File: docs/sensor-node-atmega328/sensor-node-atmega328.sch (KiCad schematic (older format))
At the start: 11 parts, among them IC1 ATMEGA328-P, P1 CONN_01X06, SW1 SPST, U1 HTU21D, U2 nRF24L01+

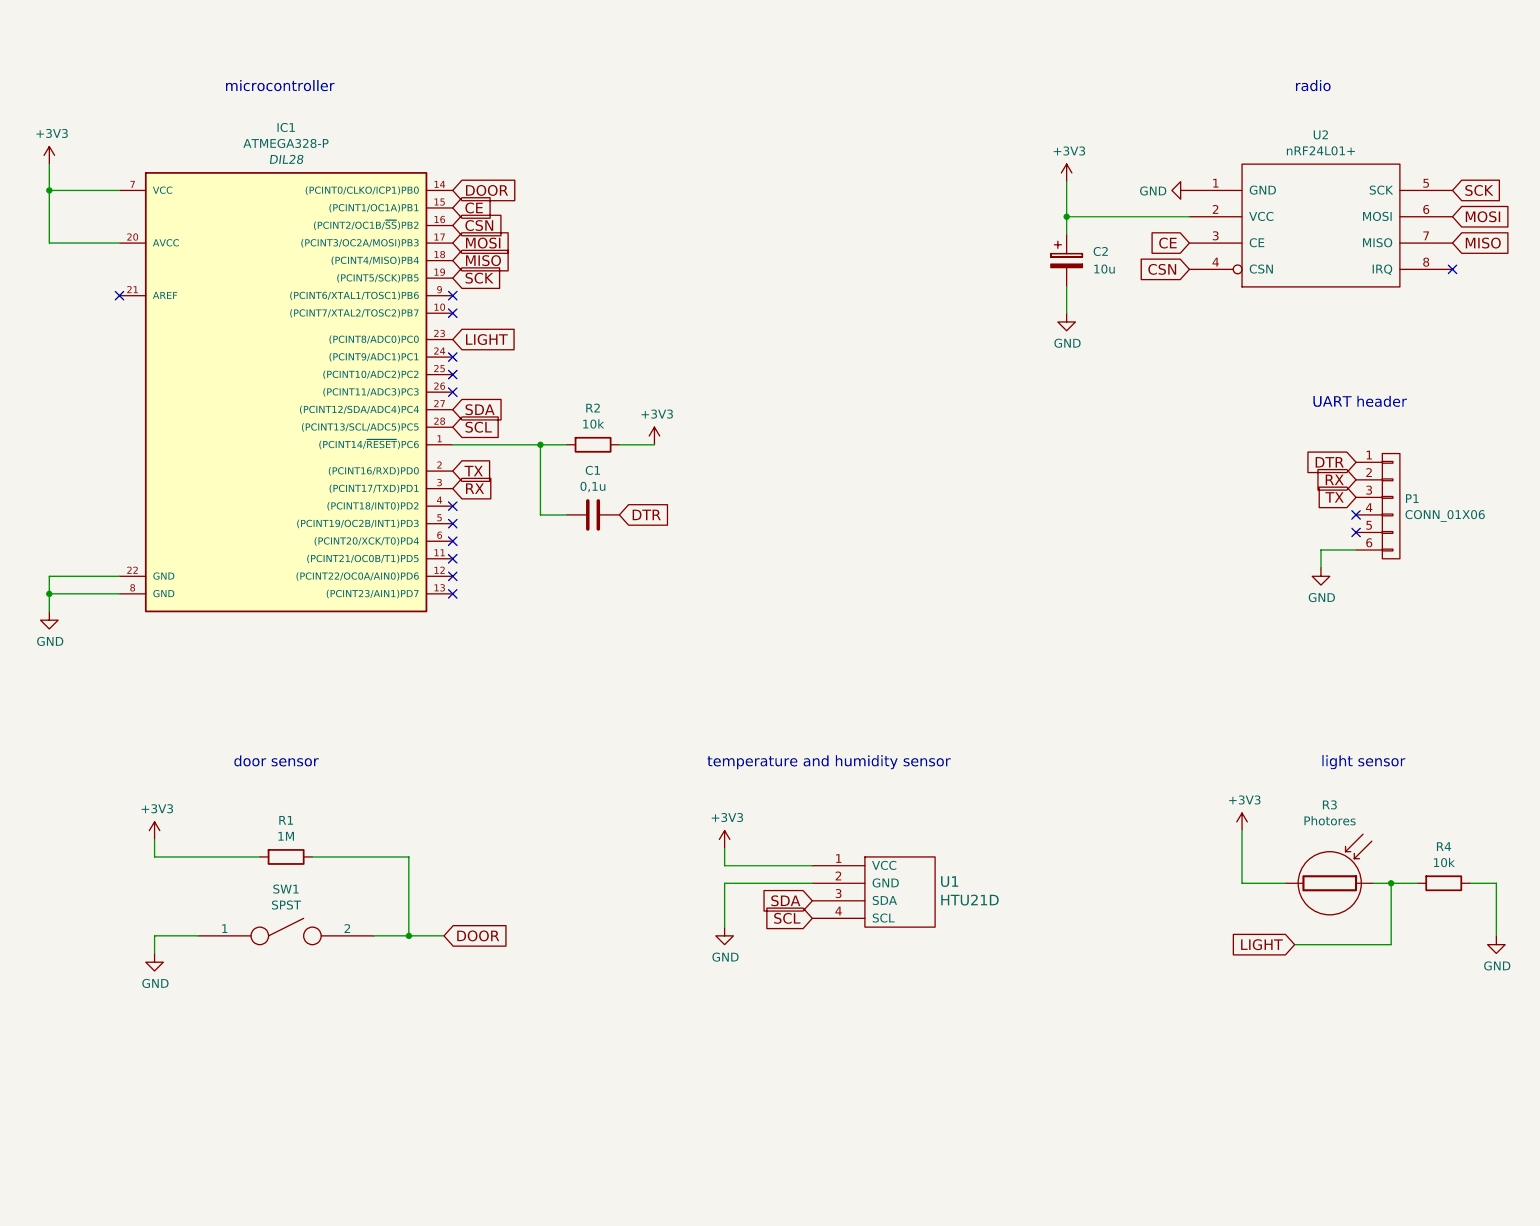
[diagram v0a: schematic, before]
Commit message: added DS18B20 temp sensor to schema
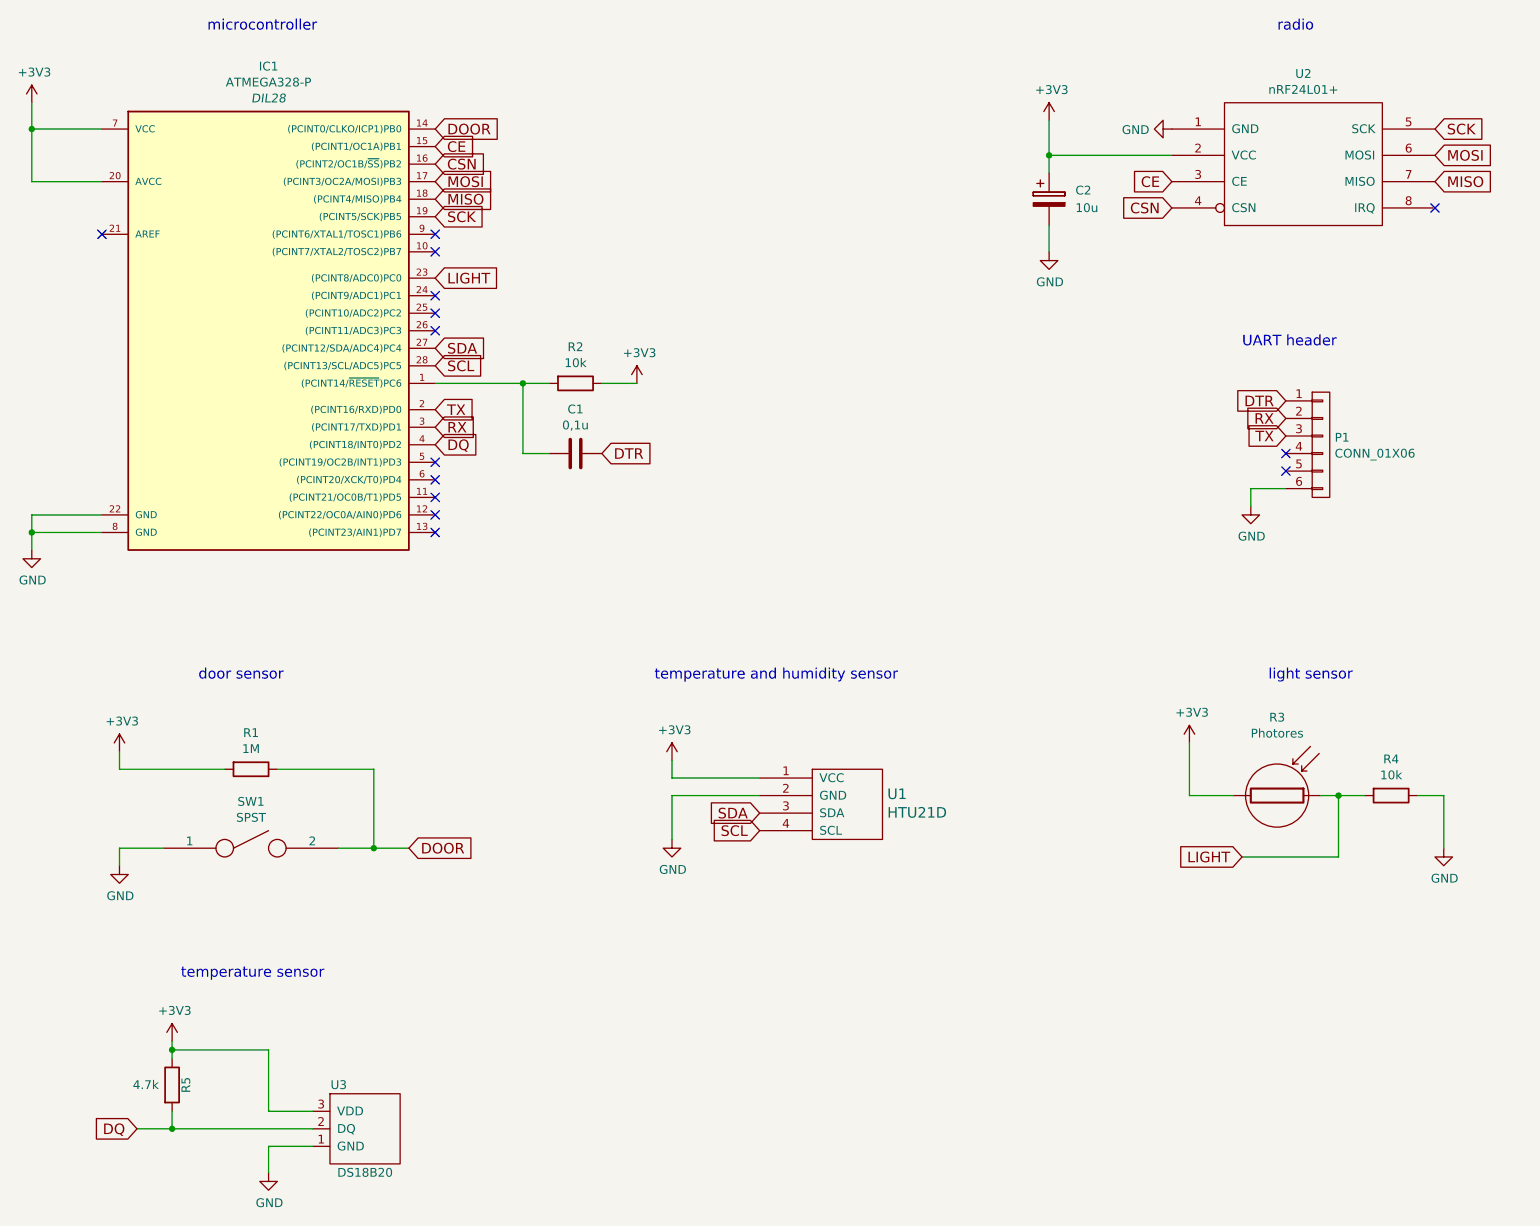
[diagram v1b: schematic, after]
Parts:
- added R5: 4.7k, symbol R
- added U3: DS18B20, symbol DS18B20
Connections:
- net +3V3: now also R5.1, U3.3 (VDD)
- net GND: now also U3.1 (GND)
- net DQ: now reaches IC1.4 ((PCINT18/INT0)PD2)
- net DQ: now also R5.2, U3.2 (DQ)
- no-connect marks 15 -> 14
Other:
- note added: "temperature sensor"
- moved on the sheet: C1, C2, IC1, P1, R1, R2, R3, R4, SW1, U1, U2
